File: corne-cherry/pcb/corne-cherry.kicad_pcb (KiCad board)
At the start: 2 copper layers, 275.5 x 105.6 mm, 172 parts, among them J1 MJ-4PP-9, J2 OLED, J3 MJ-4PP-9, J4 OLED, SW1 SW_PUSH, SW10 SW_PUSH, SW11 SW_PUSH, SW12 SW_PUSH, SW13 SW_PUSH, SW14 SW_PUSH, SW15 SW_PUSH, SW16 SW_PUSH, SW17 SW_PUSH, SW18 SW_PUSH, SW19 SW_PUSH, SW2 SW_PUSH, SW20 SW_PUSH, SW21 SW_PUSH, SW22 SW_PUSH, SW23 SW_PUSH, SW24 SW_PUSH, SW25 SW_PUSH, SW26 SW_PUSH, SW27 SW_PUSH, SW28 SW_PUSH, SW29 SW_PUSH, SW3 SW_PUSH, SW30 SW_PUSH, SW31 SW_PUSH, SW32 SW_PUSH, SW33 SW_PUSH, SW34 SW_PUSH, SW35 SW_PUSH, SW36 SW_PUSH, SW37 SW_PUSH, SW38 SW_PUSH, SW39 SW_PUSH, SW4 SW_PUSH, SW40 SW_PUSH, SW41 SW_PUSH, SW42 SW_PUSH, SW5 SW_PUSH, SW6 SW_PUSH, SW7 SW_PUSH, SW8 SW_PUSH, SW9 SW_PUSH, U1 ProMicro, U2 ProMicro

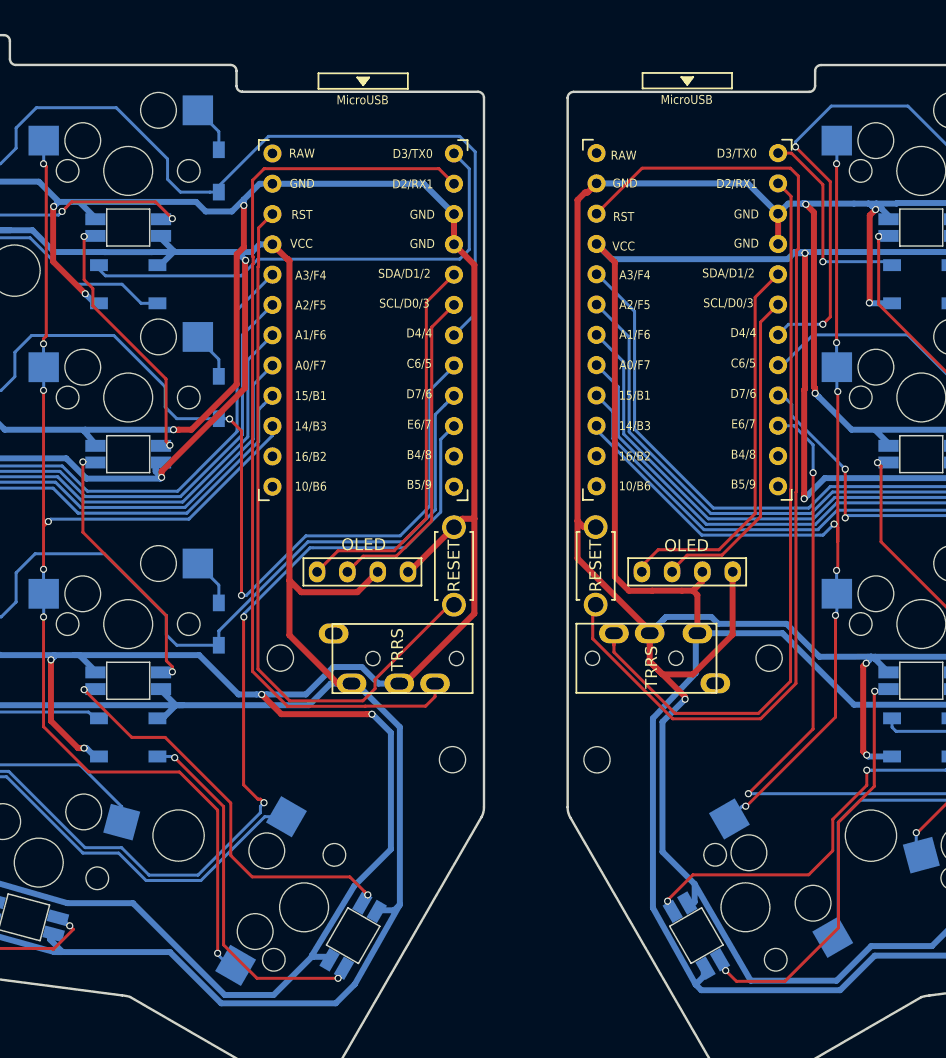
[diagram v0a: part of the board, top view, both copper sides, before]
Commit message: first commit with support for nice!nano, battery connector and power switch
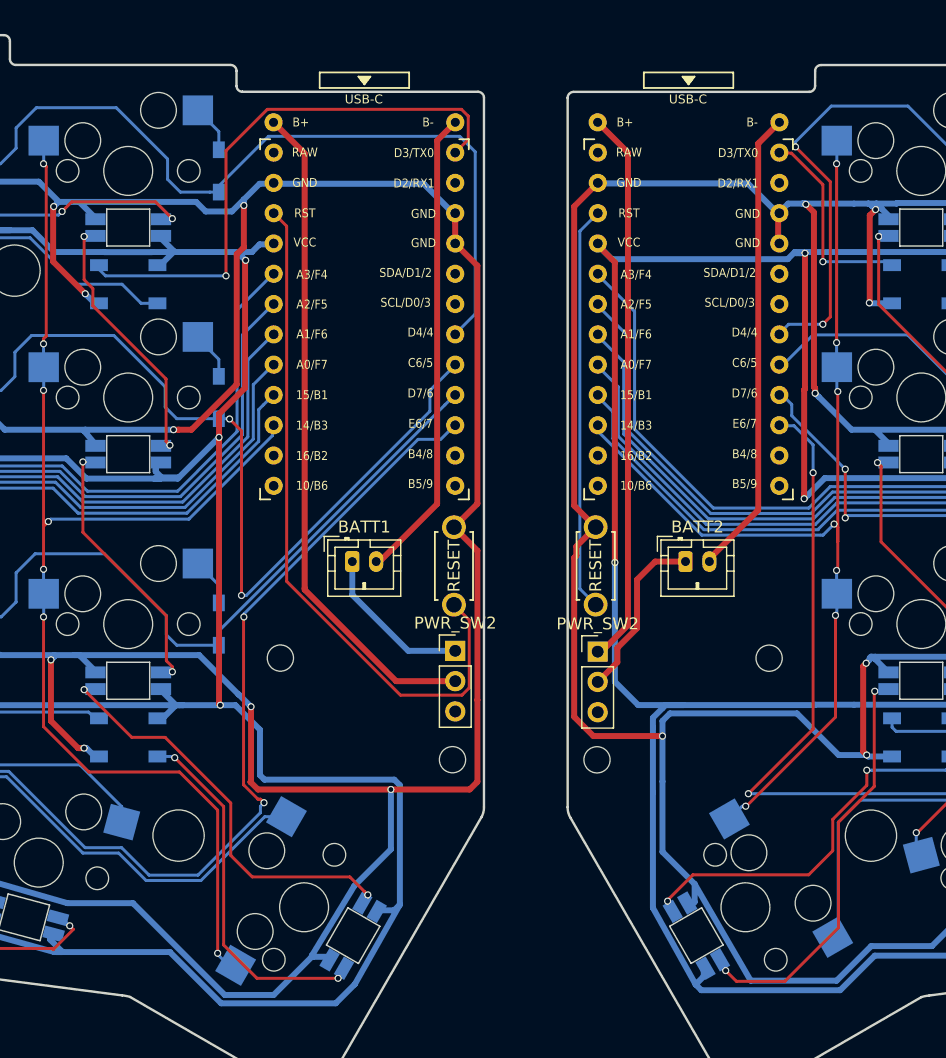
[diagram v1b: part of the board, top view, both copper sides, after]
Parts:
- removed J1, J3: MJ-4PP-9, kbd:MJ-4PP-9_1side
- removed J2, J4: OLED, kbd:OLED_1side
- removed the U1 at (134.8, 46.4)
- removed U2: ProMicro, kbd:ProMicro_v3
- added BATT1: JST_PH_B2B-PH-K_1x02_P2.00mm_Vertical, Connector_JST:JST_PH_B2B-PH-K_1x02_P2.00mm_Vertical, F.Cu at (133.9, 66.2)
- added BATT2: JST_PH_B2B-PH-K_1x02_P2.00mm_Vertical, Connector_JST:JST_PH_B2B-PH-K_1x02_P2.00mm_Vertical, F.Cu at (161.8, 66.2)
- added PWR_SW2: PinHeader_1x03_P2.54mm_Vertical, Connector_PinHeader_2.54mm:PinHeader_1x03_P2.54mm_Vertical, F.Cu at (142.5, 73.6)
- added PWR_SW2: PinHeader_1x03_P2.54mm_Vertical, Connector_PinHeader_2.54mm:PinHeader_1x03_P2.54mm_Vertical, F.Cu at (154.5, 73.7)
- added U1: nice_nano, kbd:nice_nano, F.Cu at (154.5, 31.9)
- added U1: nice_nano, kbd:nice_nano, F.Cu at (127.3, 31.9)
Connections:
- SW21 pad 1: col5 -> (no net)
- SW21 pad 2: Net-(D21-Pad2) -> (no net)
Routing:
- net (no net): track 0.00 -> 209.9 mm
- net data: track 77.0 -> 0.00 mm
- net data_r: track 62.9 -> 0.00 mm
- net reset_r: track 85.4 -> 34.1 mm
- net SDA_r: track 32.7 -> 0.00 mm
- net SDA: track 32.4 -> 0.00 mm
- net SCL_r: track 27.9 -> 0.00 mm
- net SCL: track 27.7 -> 0.00 mm
- net VCC: track 544.3 -> 518.8 mm, vias 2 -> 3
- net GNDA: track 617.9 -> 605.2 mm
- net LED: track 41.1 -> 47.2 mm, vias 0 -> 1
- net row2: track 180.7 -> 176.0 mm
- net row1: track 193.3 -> 188.7 mm
- net VDD: track 573.1 -> 568.9 mm, vias 2 -> 3
- net row3: track 121.7 -> 118.1 mm
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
